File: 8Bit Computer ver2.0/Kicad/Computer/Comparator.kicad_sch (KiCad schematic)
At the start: 9 parts, among them IC47 SN74AHC74DR, IC48 SN74AHC08DR, IC49 SN74HC682N, IC52 SN74LVC1G14DBVR, IC53 SN74LVC1G14DBVR, IC54 SN74LVC1G08DBVR, IC55 SN74LVC1G14DBVR, IC56 SN74HCS4075DR, IC57 SN74ABT574ADWR

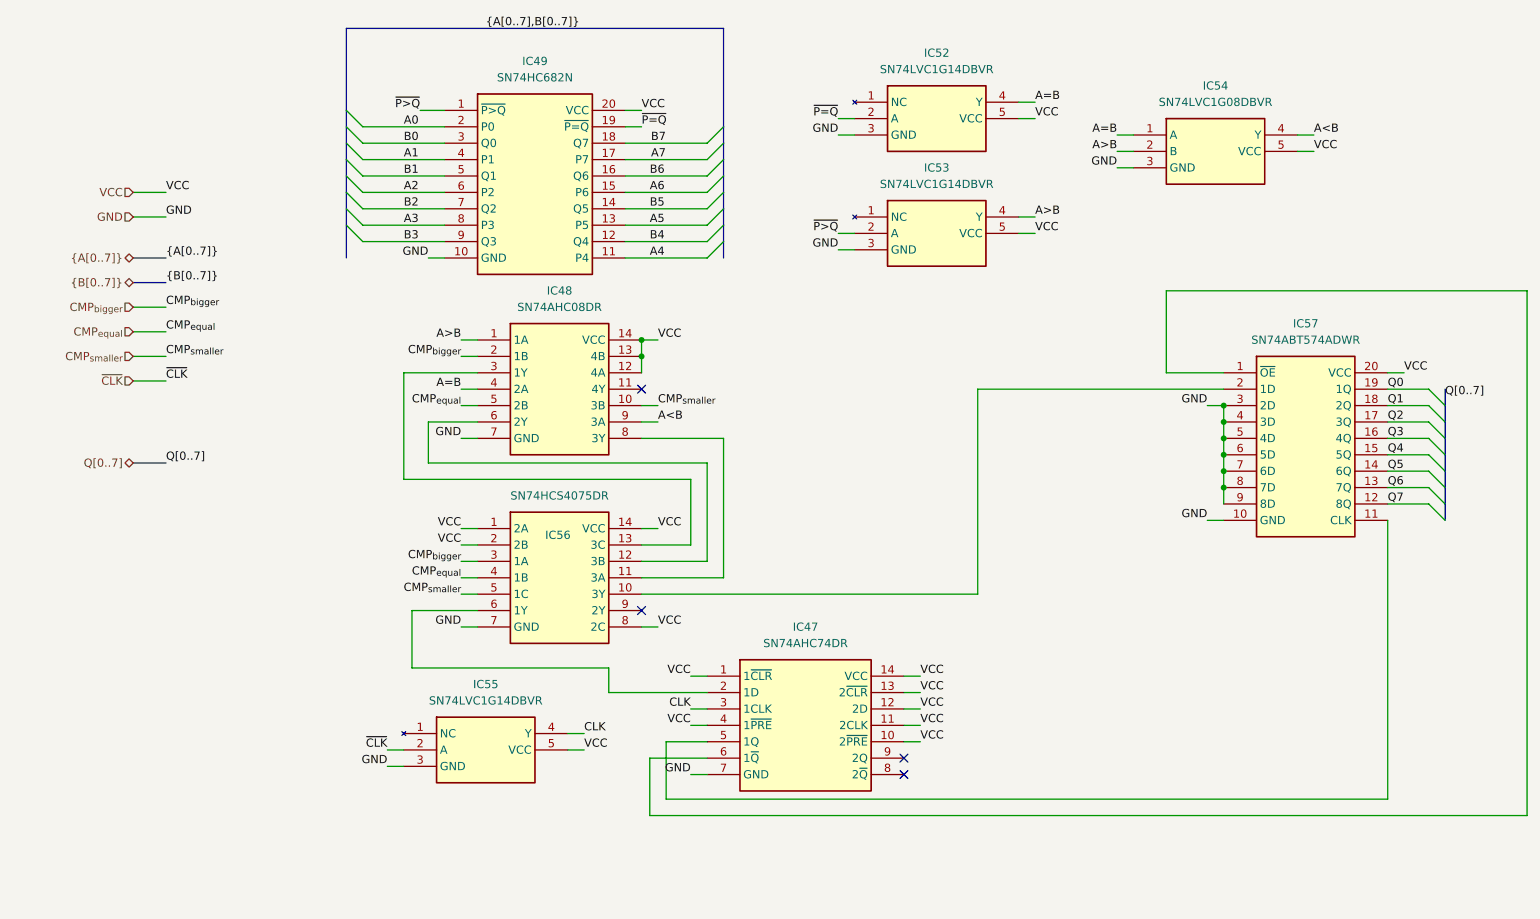
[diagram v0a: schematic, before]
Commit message: Kicad, parts
Parts:
added Leds
Kicad:
added Input Output
changed Q bus to DAT bus
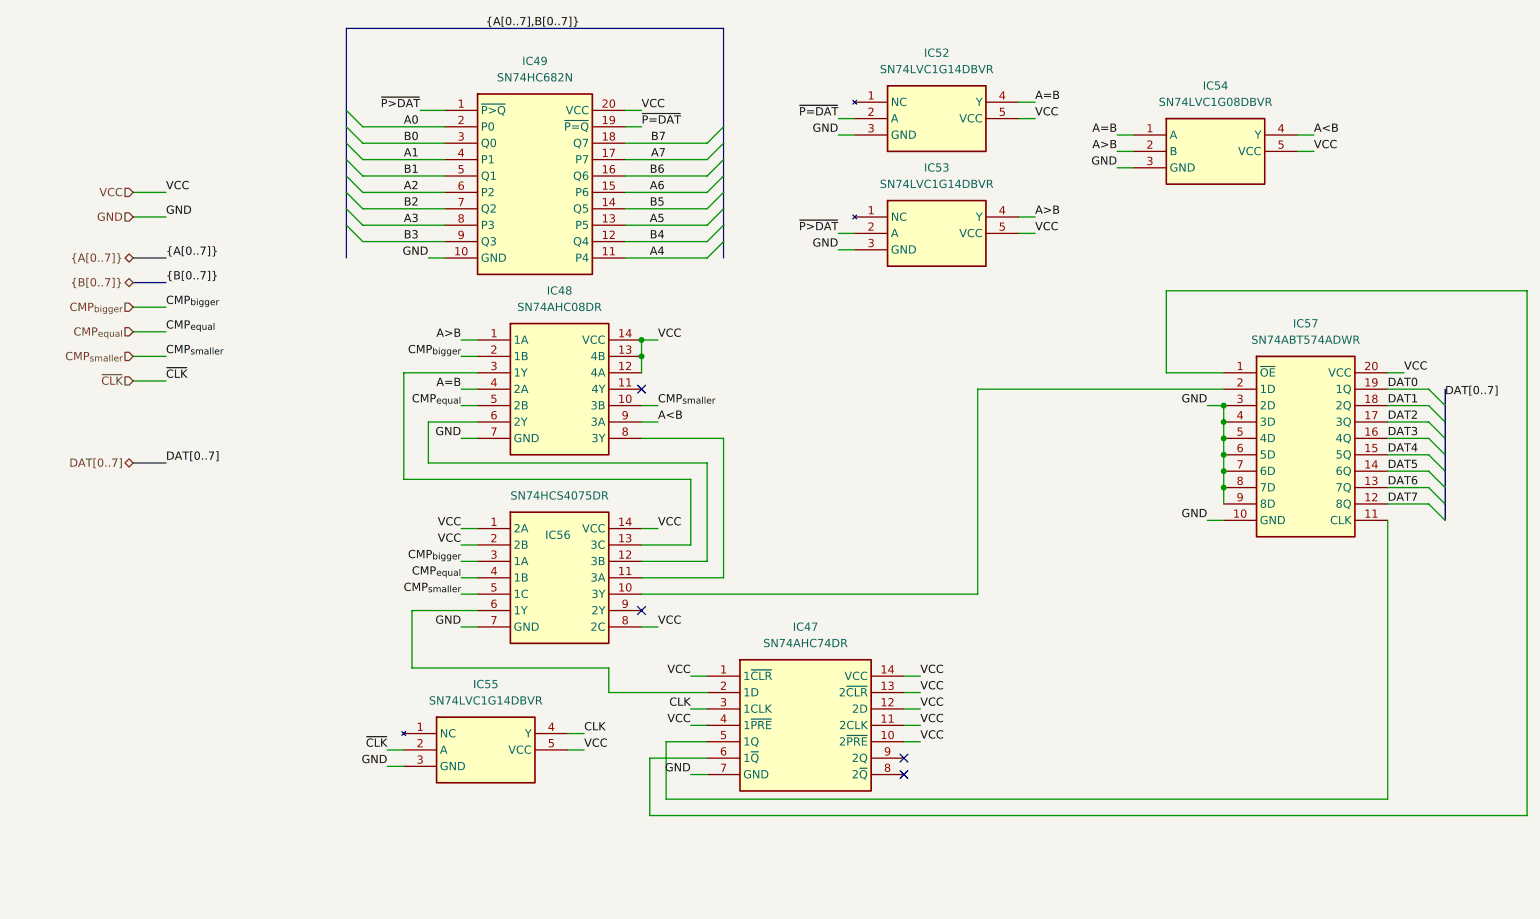
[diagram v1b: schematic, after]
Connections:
- net Q0 renamed DAT0
- net Q1 renamed DAT1
- net Q2 renamed DAT2
- net Q3 renamed DAT3
- net Q4 renamed DAT4
- net Q5 renamed DAT5
- net Q6 renamed DAT6
- net Q7 renamed DAT7
- net ~{P=Q} renamed ~{P=DAT}
- net ~{P>Q} renamed ~{P>DAT}
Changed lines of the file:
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@@
 		)
 	)
-	(label "Q1"
+	(label "DAT1"
 		(at 229.87 72.39 0)
 		(effects
@@
 		)
 	)
-	(label "Q5"
+	(label "DAT5"
 		(at 229.87 82.55 0)
 		(effects
@@
 		)
 	)
-	(label "Q2"
+	(label "DAT2"
 		(at 229.87 74.93 0)
 		(effects
@@
 		)
 	)
-	(label "Q6"
+	(label "DAT6"
 		(at 229.87 85.09 0)
 		(effects
@@
 		)
 	)
-	(label "~{P>Q}"
+	(label "~{P>DAT}"
 		(at 144.78 45.72 180)
 		(effects
@@
 		)
 	)
-	(label "Q0"
+	(label "DAT0"
 		(at 229.87 69.85 0)
 		(effects
@@
 		)
 	)
-	(label "Q3"
+	(label "DAT3"
 		(at 229.87 77.47 0)
 		(effects
@@
 		)
 	)
-	(label "~{P>Q}"
+	(label "~{P>DAT}"
 		(at 80.01 26.67 180)
 		(effects
@@
 		)
 	)
-	(label "Q7"
+	(label "DAT7"
 		(at 229.87 87.63 0)
 		(effects
@@
 		)
 	)
-	(label "Q[0..7]"
+	(label "DAT[0..7]"
 		(at 40.64 81.28 0)
 		(effects
@@
 		)
 	)
-	(label "Q[0..7]"
+	(label "DAT[0..7]"
 		(at 238.76 71.12 0)
 		(effects
@@
 		)
 	)
-	(label "Q4"
+	(label "DAT4"
 		(at 229.87 80.01 0)
 		(effects
@@
 		)
 	)
-	(label "~{P=Q}"
+	(label "~{P=DAT}"
 		(at 114.3 29.21 0)
 		(effects
@@
 		)
 	)
-	(label "~{P=Q}"
+	(label "~{P=DAT}"
 		(at 144.78 27.94 180)
 		(effects
@@
 		)
 	)
-	(hierarchical_label "Q[0..7]"
+	(hierarchical_label "DAT[0..7]"
 		(shape tri_state)
 		(at 35.56 81.28 180)

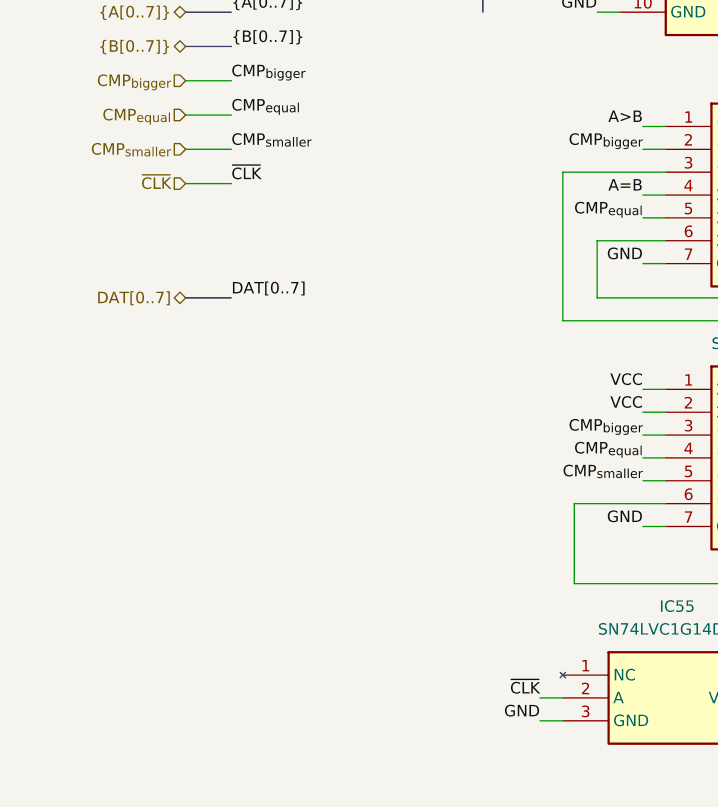
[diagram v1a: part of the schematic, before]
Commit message: Kicad, parts
parts:
added USB C PD Triggerboard
added Delay Chip for 90ns
added Push Button
Kicad:
added USB C PD Triggerboard
added rising edge detector via Delay and Xor for Accept Push Button
added VBUS net
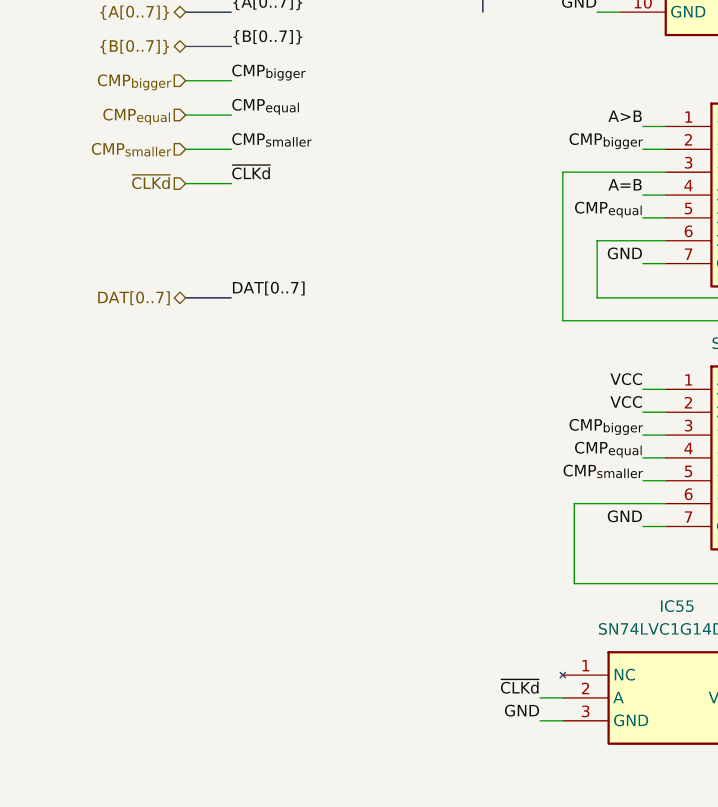
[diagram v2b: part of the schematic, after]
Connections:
- net ~{CLK} renamed ~{CLKd}
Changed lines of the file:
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@@
 		)
 	)
-	(label "~{CLK}"
+	(label "~{CLKd}"
 		(at 40.64 68.58 0)
 		(effects
@@
 		)
 	)
-	(label "~{CLK}"
+	(label "~{CLKd}"
 		(at 74.93 125.73 180)
 		(effects
@@
 		)
 	)
-	(hierarchical_label "~{CLK}"
+	(hierarchical_label "~{CLKd}"
 		(shape input)
 		(at 35.56 68.58 180)

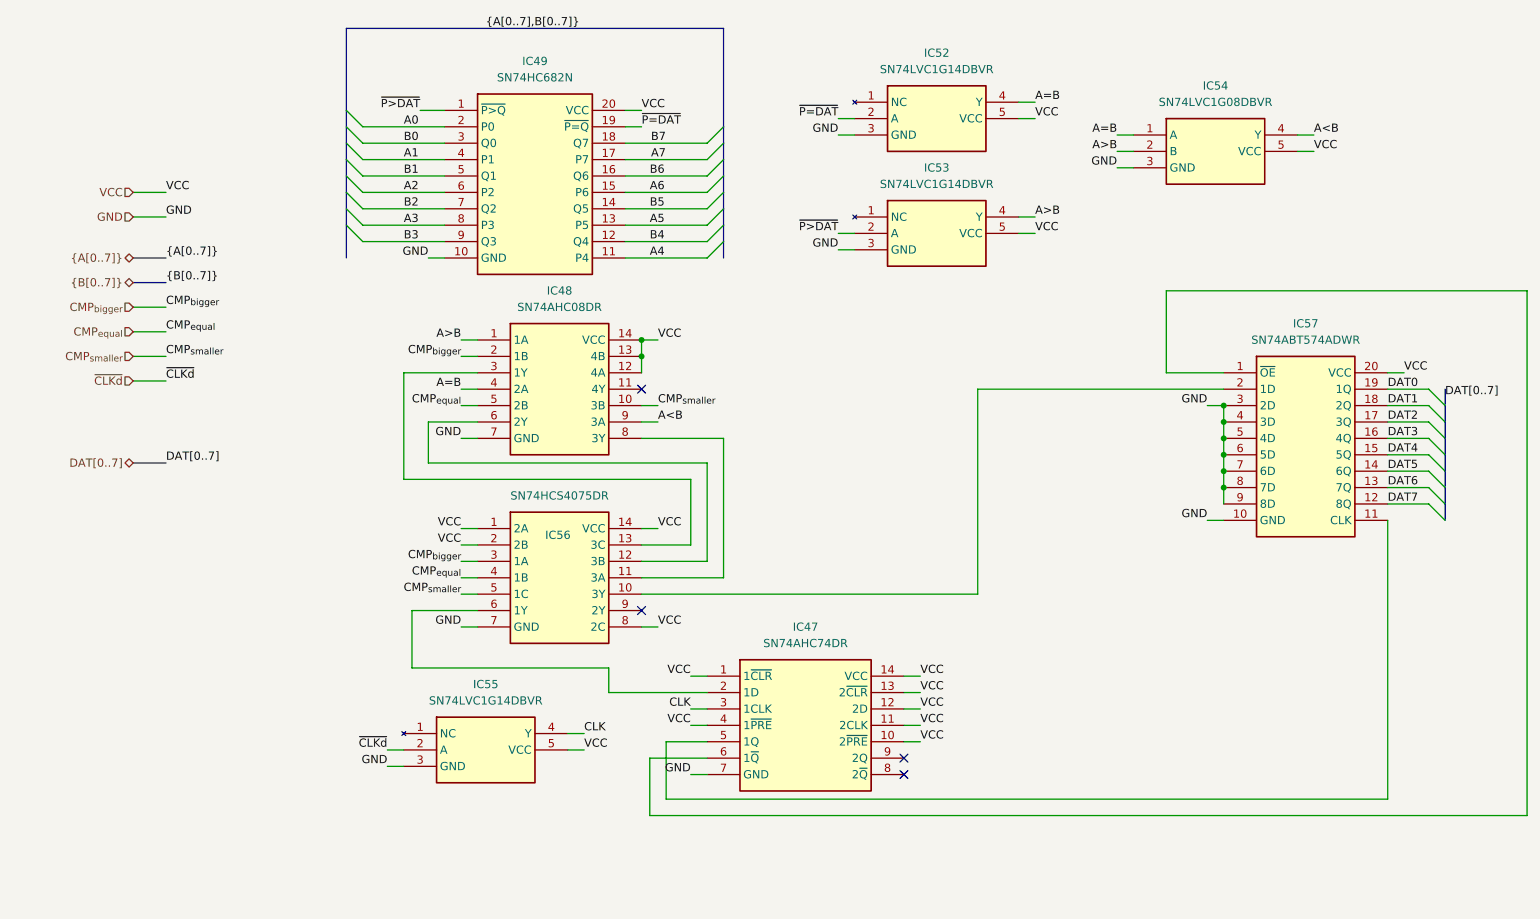
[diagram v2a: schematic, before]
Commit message: Kicad SCH/PCB
Kicad SCH/PCB:
changed the References in SCH
began with INOUTPUT module nearly done
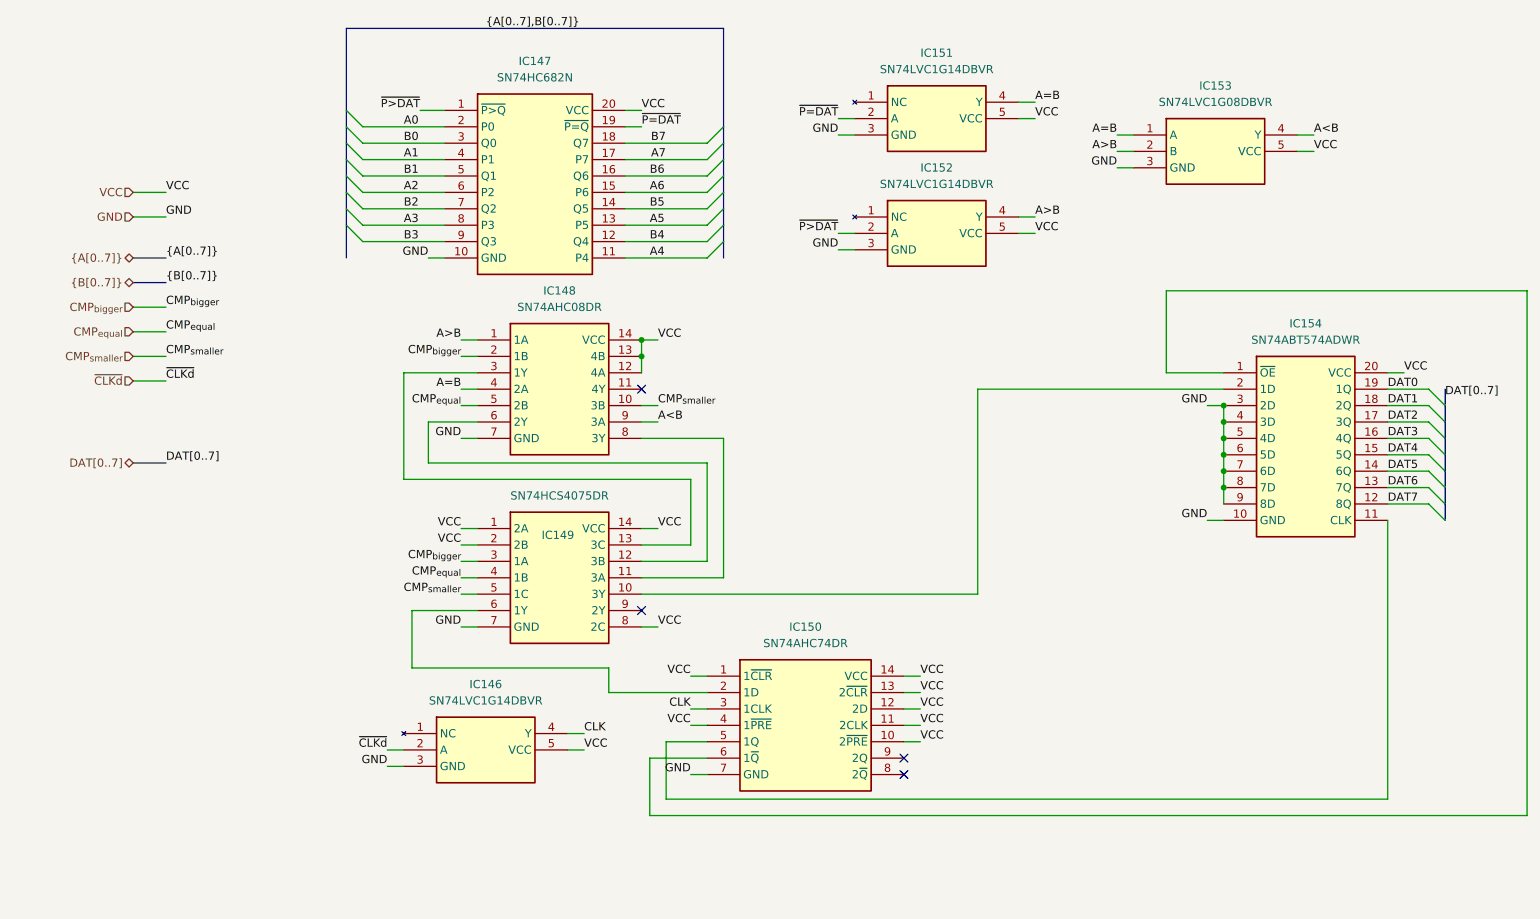
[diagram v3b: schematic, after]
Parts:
- renumbered IC55 to IC146, IC49 to IC147, IC48 to IC148, IC56 to IC149, IC47 to IC150, IC52 to IC151, IC53 to IC152, IC54 to IC153, IC57 to IC154
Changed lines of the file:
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@@
 		(dnp no)
 		(fields_autoplaced yes)
-		(property "Reference" "IC53"
+		(property "Reference" "IC152"
 			(at 160.02 35.56 0)
 			(effects
@@
 			(project "Computer"
 				(path "/1196a00e-6878-4d6d-82b7-9e052dfe7c14/c4d8b530-1c6d-45af-88d2-7dc1d4321a34/50f55c79-2069-4dac-a92a-a304de2499f6"
-					(reference "IC53")
+					(reference "IC152")
 					(unit 1)
 				)
@@
 		(on_board yes)
 		(dnp no)
-		(property "Reference" "IC56"
+		(property "Reference" "IC149"
 			(at 101.346 92.456 0)
 			(effects
@@
 			(project ""
 				(path "/1196a00e-6878-4d6d-82b7-9e052dfe7c14/c4d8b530-1c6d-45af-88d2-7dc1d4321a34/50f55c79-2069-4dac-a92a-a304de2499f6"
-					(reference "IC56")
+					(reference "IC149")
 					(unit 1)
 				)
@@
 		(dnp no)
 		(fields_autoplaced yes)
-		(property "Reference" "IC54"
+		(property "Reference" "IC153"
 			(at 203.2 22.86 0)
 			(effects
@@
 			(project ""
 				(path "/1196a00e-6878-4d6d-82b7-9e052dfe7c14/c4d8b530-1c6d-45af-88d2-7dc1d4321a34/50f55c79-2069-4dac-a92a-a304de2499f6"
-					(reference "IC54")
+					(reference "IC153")
 					(unit 1)
 				)
@@
 		(dnp no)
 		(fields_autoplaced yes)
-		(property "Reference" "IC49"
+		(property "Reference" "IC147"
 			(at 97.79 19.05 0)
 			(effects
@@
 			(project ""
 				(path "/1196a00e-6878-4d6d-82b7-9e052dfe7c14/c4d8b530-1c6d-45af-88d2-7dc1d4321a34/50f55c79-2069-4dac-a92a-a304de2499f6"
-					(reference "IC49")
+					(reference "IC147")
 					(unit 1)
 				)
@@
 		(dnp no)
 		(fields_autoplaced yes)
-		(property "Reference" "IC52"
+		(property "Reference" "IC151"
 			(at 160.02 17.78 0)
 			(effects
@@
 			(project ""
 				(path "/1196a00e-6878-4d6d-82b7-9e052dfe7c14/c4d8b530-1c6d-45af-88d2-7dc1d4321a34/50f55c79-2069-4dac-a92a-a304de2499f6"
-					(reference "IC52")
+					(reference "IC151")
 					(unit 1)
 				)
@@
 		(on_board yes)
 		(dnp no)
-		(property "Reference" "IC55"
+		(property "Reference" "IC146"
 			(at 90.17 115.57 0)
 			(effects
@@
 			(project ""
 				(path "/1196a00e-6878-4d6d-82b7-9e052dfe7c14/c4d8b530-1c6d-45af-88d2-7dc1d4321a34/50f55c79-2069-4dac-a92a-a304de2499f6"
-					(reference "IC55")
+					(reference "IC146")
 					(unit 1)
 				)
@@
 		(dnp no)
 		(fields_autoplaced yes)
-		(property "Reference" "IC57"
+		(property "Reference" "IC154"
 			(at 217.17 59.69 0)
 			(effects
@@
 			(project "Computer"
 				(path "/1196a00e-6878-4d6d-82b7-9e052dfe7c14/c4d8b530-1c6d-45af-88d2-7dc1d4321a34/50f55c79-2069-4dac-a92a-a304de2499f6"
-					(reference "IC57")
+					(reference "IC154")
 					(unit 1)
 				)
@@
 		(dnp no)
 		(fields_autoplaced yes)
-		(property "Reference" "IC47"
+		(property "Reference" "IC150"
 			(at 139.7 106.68 0)
 			(effects
@@
 			(project ""
 				(path "/1196a00e-6878-4d6d-82b7-9e052dfe7c14/c4d8b530-1c6d-45af-88d2-7dc1d4321a34/50f55c79-2069-4dac-a92a-a304de2499f6"
-					(reference "IC47")
+					(reference "IC150")
 					(unit 1)
 				)
@@
 		(dnp no)
 		(fields_autoplaced yes)
-		(property "Reference" "IC48"
+		(property "Reference" "IC148"
 			(at 101.6 54.61 0)
 			(effects
@@
 			(project ""
 				(path "/1196a00e-6878-4d6d-82b7-9e052dfe7c14/c4d8b530-1c6d-45af-88d2-7dc1d4321a34/50f55c79-2069-4dac-a92a-a304de2499f6"
-					(reference "IC48")
+					(reference "IC148")
 					(unit 1)
 				)

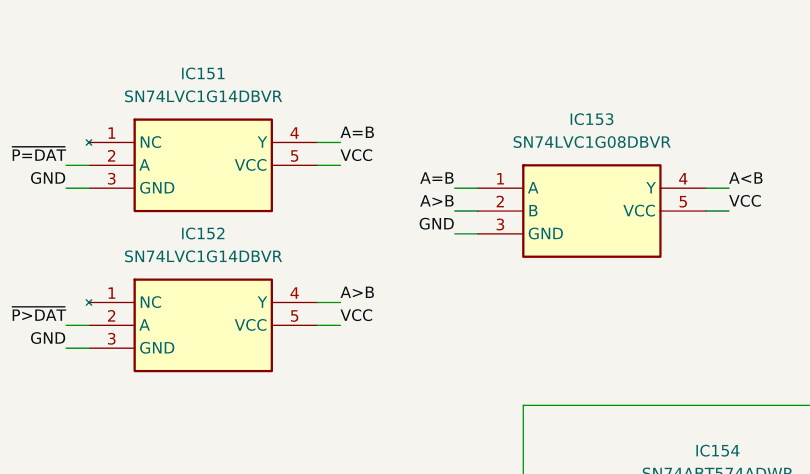
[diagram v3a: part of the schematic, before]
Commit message: Kicad Fixes only schematic
fixed important schematic errors
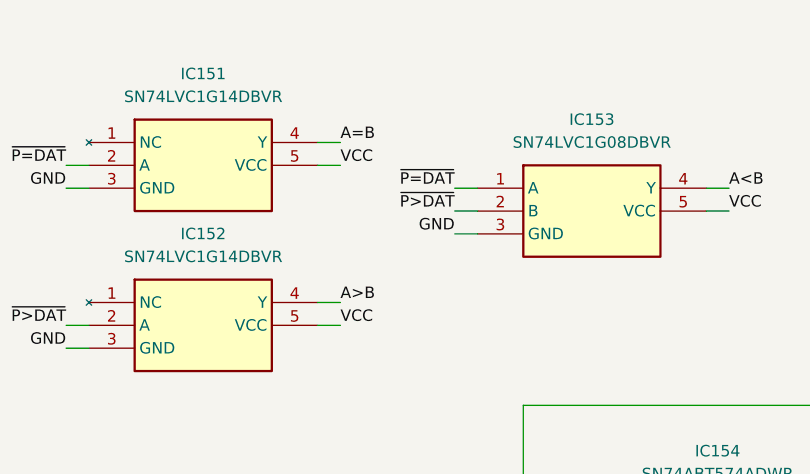
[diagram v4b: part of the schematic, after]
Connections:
- net A=B: no longer IC153.1 (A)
- net A>B: no longer IC153.2 (B)
- net ~{P=DAT}: now also IC153.1 (A)
- net ~{P>DAT}: now also IC153.2 (B)
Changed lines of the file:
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@@
+		)
+	)
+	(label "~{P>DAT}"
+		(at 187.96 33.02 180)
+		(effects
+			(font
+				(size 1.27 1.27)
+			)
+			(justify right bottom)
 		)
 	)
@@
 		)
 	)
-	(label "A>B"
-		(at 187.96 33.02 180)
-		(effects
-			(font
-				(size 1.27 1.27)
-			)
-			(justify right bottom)
-		)
-	)
 	(label "GND"
 		(at 144.78 30.48 180)
@@
 		)
 	)
-	(label "A=B"
+	(label "~{P=DAT}"
 		(at 187.96 30.48 180)
 		(effects
